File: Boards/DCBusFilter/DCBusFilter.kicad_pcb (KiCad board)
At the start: 4 copper layers, 89 x 81 mm, 8 parts, among them J1 TBP01R2-508-04BE, J2 TBP01R2-508-04BE

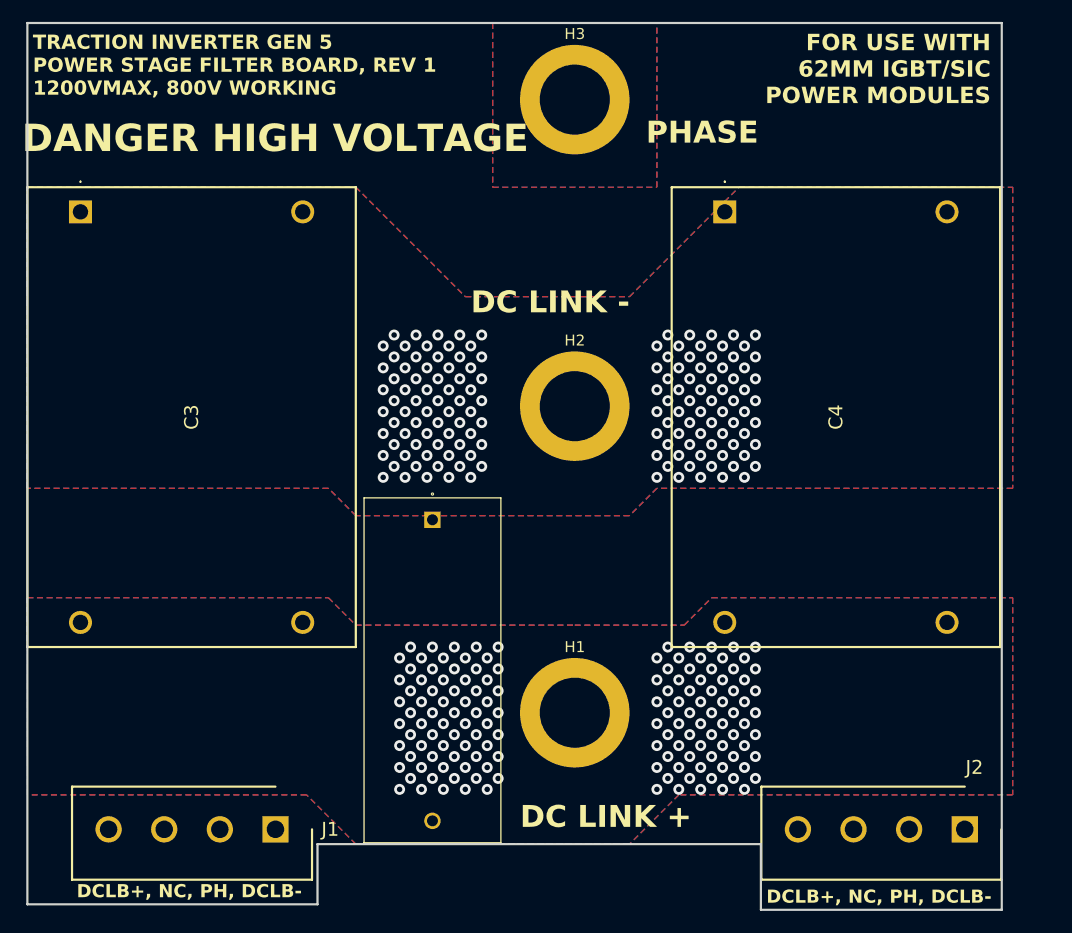
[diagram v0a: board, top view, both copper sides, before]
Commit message: layout control boards, add baseplate, refine mechanical layout
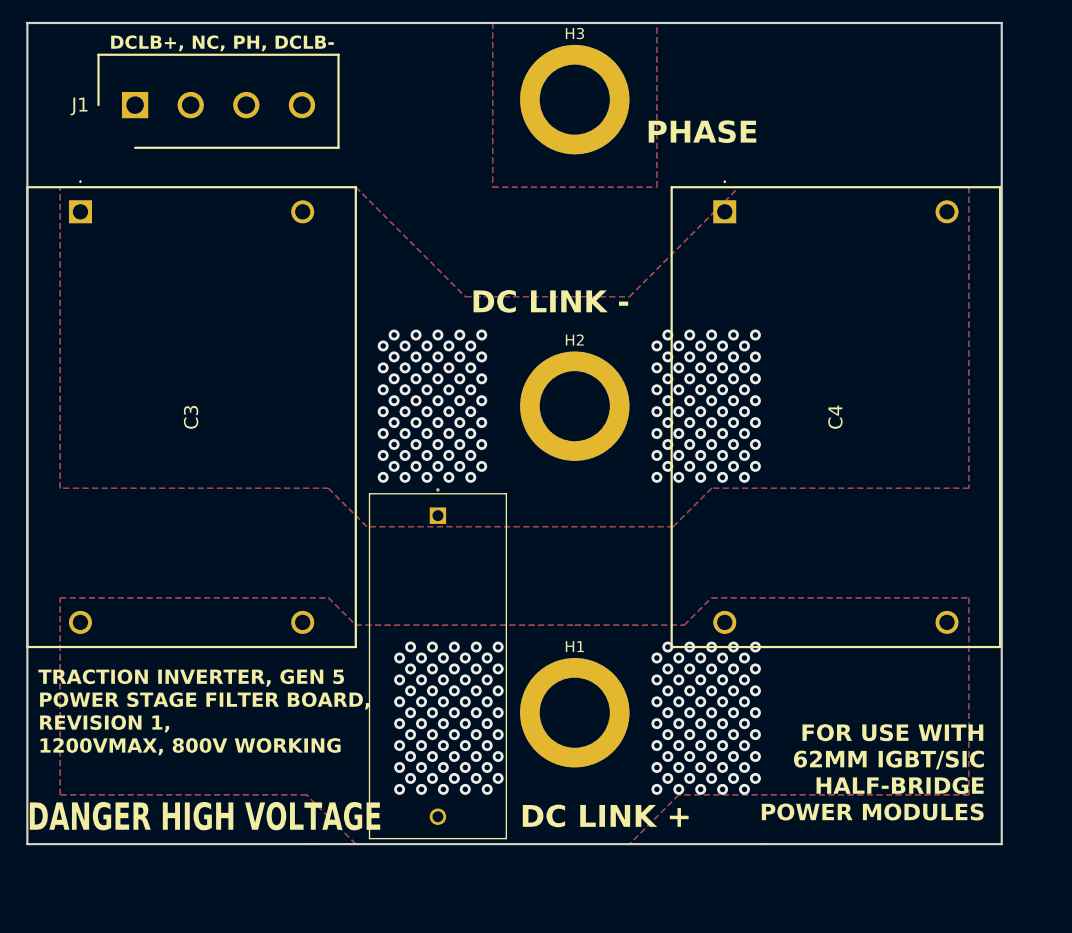
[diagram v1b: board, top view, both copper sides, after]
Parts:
- removed J2: TBP01R2-508-04BE, InverterCom:SHDR4W100P0X508_1X4_2192X850X1200P
- moved J1 67.4 mm to (9.84, 7.50), turned to 0 degrees
- moved C1 0.62 mm to (37.5, 45.0)
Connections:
- J1 pad 1: /DC_LINK_- -> /DC_LINK_+
- J1 pad 2: /PHASE_LEG -> unconnected-(J1-Pad2)
- J1 pad 3: unconnected-(J1-Pad3) -> /PHASE_LEG
- J1 pad 4: /DC_LINK_+ -> /DC_LINK_-
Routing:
- net /PHASE_LEG: track 173.7 -> 38.7 mm
- net /DC_LINK_-: track 96.7 -> 10.7 mm
- net /DC_LINK_+: track 44.0 -> 49.4 mm
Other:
- board size 89 x 81 mm -> 89 x 75 mm
- board text added: "FOR USE WITH 62MM IGBT/SIC HALF-BRIDGE POWER MODULES"
- board text added: "TRACTION INVERTER, GEN 5 POWER STAGE FILTER BOARD, REVISION 1, 1200VMAX, 800V WORKING"
- board text removed: "FOR USE WITH 62MM IGBT/SIC POWER MODULES"
- board text removed: "TRACTION INVERTER GEN 5 POWER STAGE FILTER BOARD, REV 1 1200VMAX, 800V WORKING"

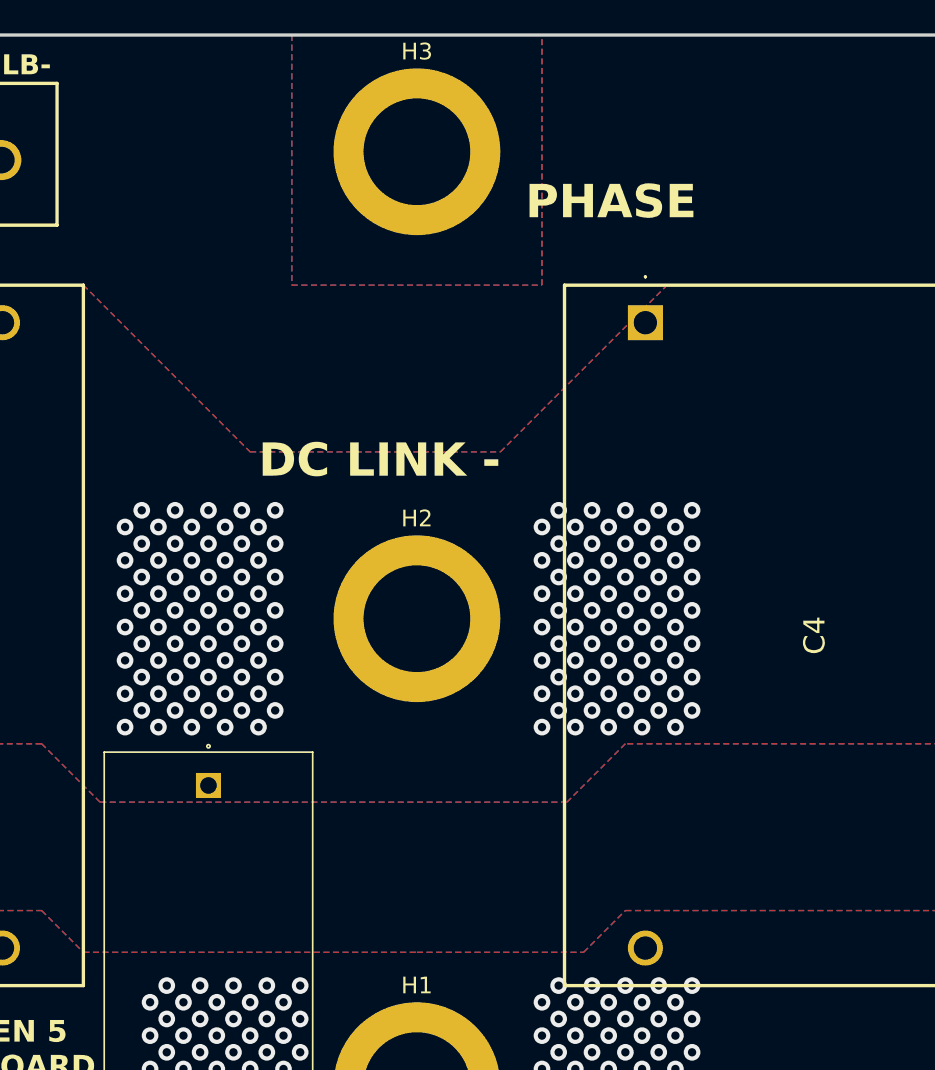
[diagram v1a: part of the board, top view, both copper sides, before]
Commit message: Layout mainboard, add EMI filter caps
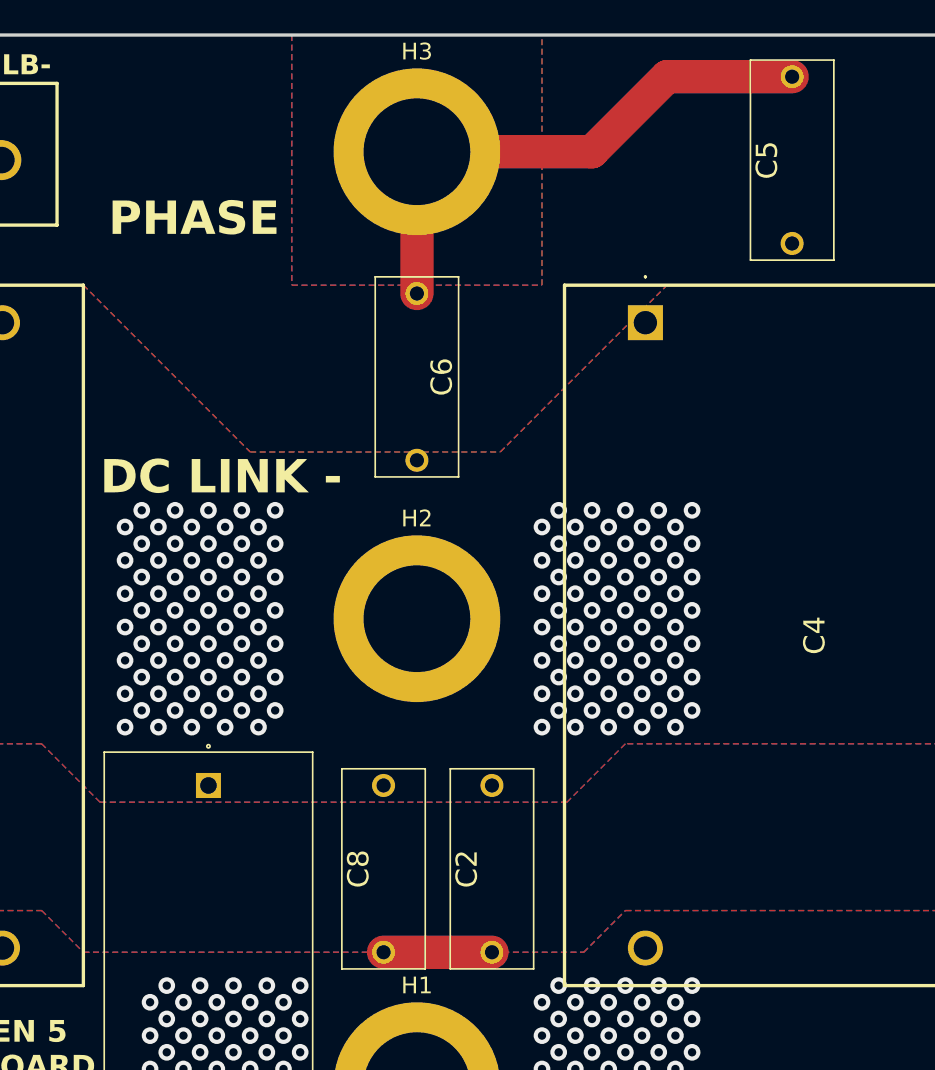
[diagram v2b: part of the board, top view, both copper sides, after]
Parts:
- added C2: VY1222M47Y5UQ6TV0, InverterCom:VY1222M47Y5UQ6TV0, F.Cu at (54.5, 45.0)
- added C5: VY1222M47Y5UQ6TV0, InverterCom:VY1222M47Y5UQ6TV0, F.Cu at (72.5, 2.50)
- added C6: VY1222M47Y5UQ6TV0, InverterCom:VY1222M47Y5UQ6TV0, F.Cu at (50.0, 25.5)
- added C8: VY1222M47Y5UQ6TV0, InverterCom:VY1222M47Y5UQ6TV0, F.Cu at (48.0, 45.0)
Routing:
- net /DC_LINK_+: track 49.4 -> 101.8 mm
- net /PHASE_LEG: track 38.7 -> 71.6 mm
- net /DC_LINK_-: track 10.7 -> 9.78 mm
